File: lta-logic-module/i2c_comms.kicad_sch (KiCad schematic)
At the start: 9 parts

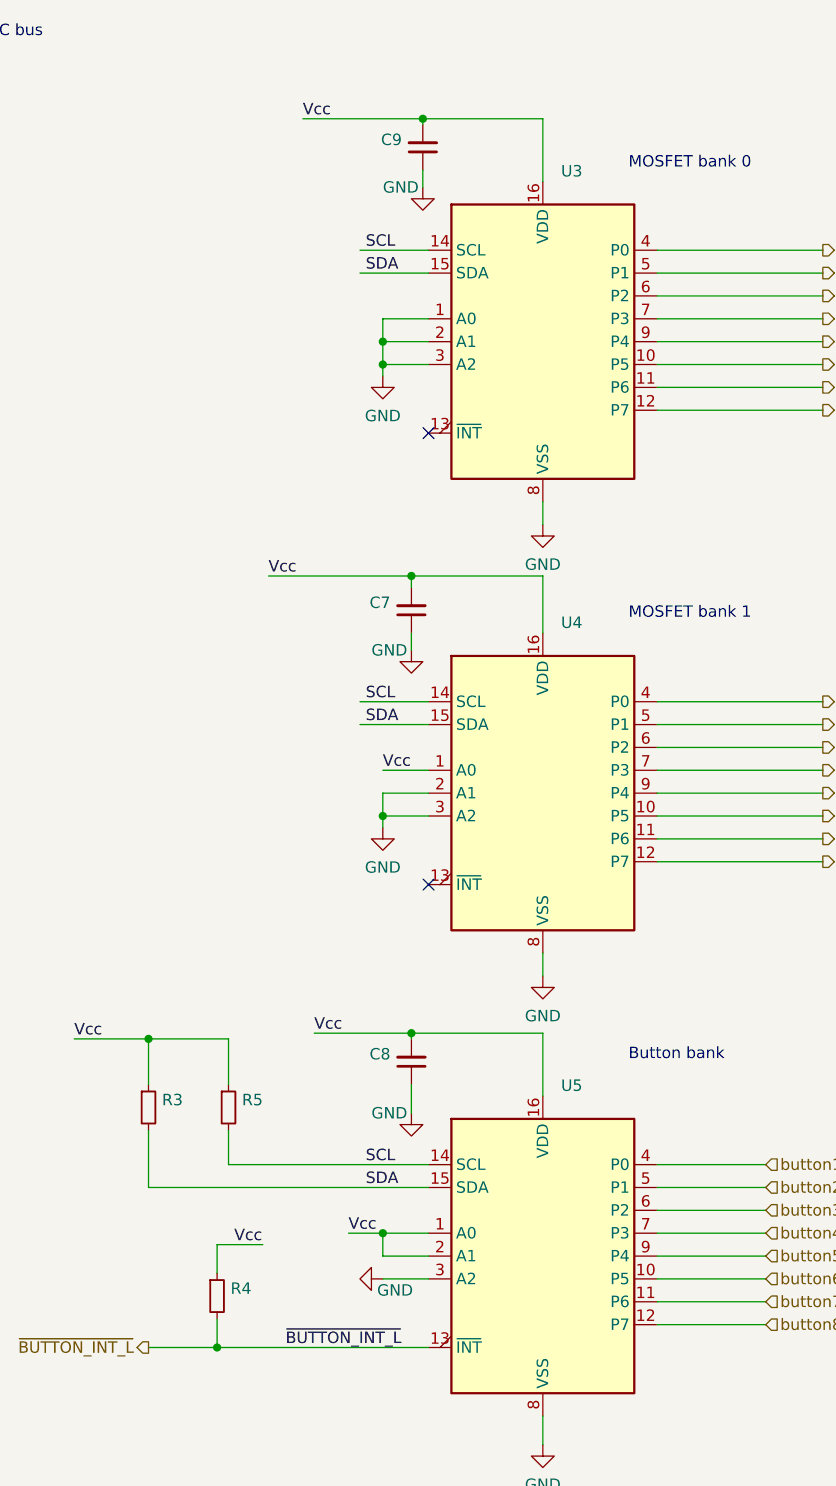
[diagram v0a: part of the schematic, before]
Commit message: Update logic module power budget from button LED measurements.
Button LEDs draw ~11mA each (98 mA total) empirically; not the ~20mA each
I initially guessed for estimating purposes.
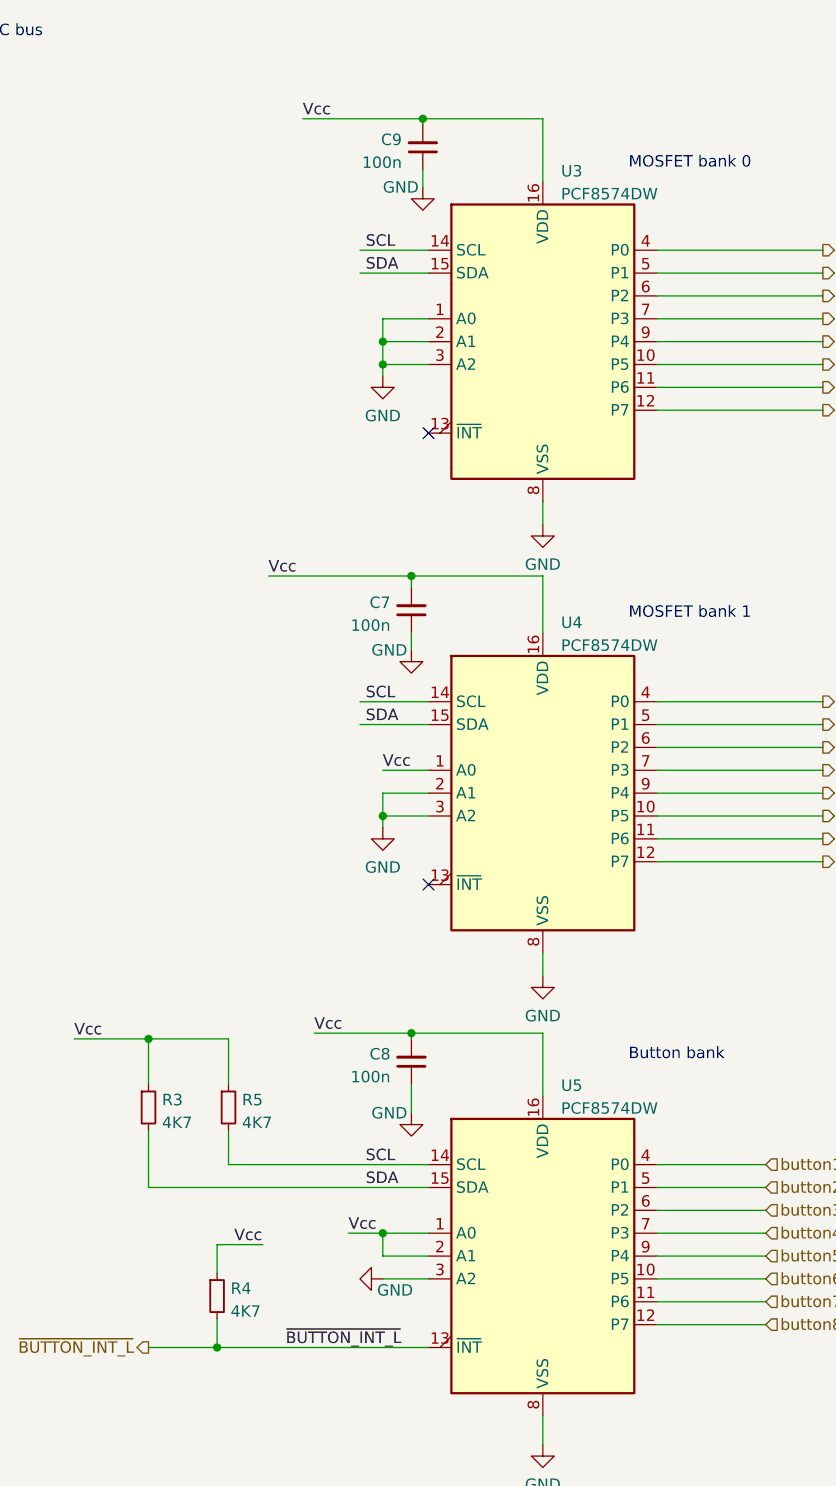
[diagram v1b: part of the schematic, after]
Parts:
- C7, C8, C9: value (none) -> 100n; footprint (none) -> Capacitor_SMD:C_0603_1608Metric
- R3, R4, R5: value (none) -> 4K7; footprint (none) -> Resistor_SMD:R_0603_1608Metric
- U3, U4, U5: value (none) -> PCF8574DW; footprint (none) -> Aaron_TI_Parts:TI_SOIC_DW0016A
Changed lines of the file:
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@@
       (effects (font (size 1.27 1.27)) (justify left))
     )
-    (property "Value" "" (id 1) (at 77.0636 137.5922 0)
-      (effects (font (size 1.27 1.27)) (justify left))
-    )
-    (property "Footprint" "" (id 2) (at 75.565 135.89 0)
+    (property "Value" "4K7" (id 1) (at 77.0636 137.5922 0)
+      (effects (font (size 1.27 1.27)) (justify left))
+    )
+    (property "Footprint" "Resistor_SMD:R_0603_1608Metric" (id 2) (at 75.565 135.89 0)
       (effects (font (size 1.27 1.27)) hide)
     )
@@
       (effects (font (size 1.27 1.27)) (justify right))
     )
-    (property "Value" "" (id 1) (at 93.5609 132.5058 0)
-      (effects (font (size 1.27 1.27)) (justify right))
-    )
-    (property "Footprint" "" (id 2) (at 95.885 130.81 0)
+    (property "Value" "100n" (id 1) (at 93.5609 132.5058 0)
+      (effects (font (size 1.27 1.27)) (justify right))
+    )
+    (property "Footprint" "Capacitor_SMD:C_0603_1608Metric" (id 2) (at 95.885 130.81 0)
       (effects (font (size 1.27 1.27)) hide)
     )
@@
       (effects (font (size 1.27 1.27)) (justify left))
     )
-    (property "Value" "" (id 1) (at 75.7936 158.5472 0)
-      (effects (font (size 1.27 1.27)) (justify left))
-    )
-    (property "Footprint" "" (id 2) (at 74.295 156.845 0)
+    (property "Value" "4K7" (id 1) (at 75.7936 158.5472 0)
+      (effects (font (size 1.27 1.27)) (justify left))
+    )
+    (property "Footprint" "Resistor_SMD:R_0603_1608Metric" (id 2) (at 74.295 156.845 0)
       (effects (font (size 1.27 1.27)) hide)
     )
@@
       (effects (font (size 1.27 1.27)) (justify right))
     )
-    (property "Value" "" (id 1) (at 93.5609 82.3408 0)
-      (effects (font (size 1.27 1.27)) (justify right))
-    )
-    (property "Footprint" "" (id 2) (at 95.885 80.645 0)
+    (property "Value" "100n" (id 1) (at 93.5609 82.3408 0)
+      (effects (font (size 1.27 1.27)) (justify right))
+    )
+    (property "Footprint" "Capacitor_SMD:C_0603_1608Metric" (id 2) (at 95.885 80.645 0)
       (effects (font (size 1.27 1.27)) hide)
     )
@@
       (effects (font (size 1.27 1.27)) (justify right))
     )
-    (property "Value" "" (id 1) (at 94.8309 30.9058 0)
-      (effects (font (size 1.27 1.27)) (justify right))
-    )
-    (property "Footprint" "" (id 2) (at 97.155 29.21 0)
+    (property "Value" "100n" (id 1) (at 94.8309 30.9058 0)
+      (effects (font (size 1.27 1.27)) (justify right))
+    )
+    (property "Footprint" "Capacitor_SMD:C_0603_1608Metric" (id 2) (at 97.155 29.21 0)
       (effects (font (size 1.27 1.27)) hide)
     )
@@
       (effects (font (size 1.27 1.27)) (justify left))
     )
-    (property "Value" "" (id 1) (at 112.5094 84.5621 0)
-      (effects (font (size 1.27 1.27)) (justify left))
-    )
-    (property "Footprint" "" (id 2) (at 110.49 100.965 0)
+    (property "Value" "PCF8574DW" (id 1) (at 112.5094 84.5621 0)
+      (effects (font (size 1.27 1.27)) (justify left))
+    )
+    (property "Footprint" "Aaron_TI_Parts:TI_SOIC_DW0016A" (id 2) (at 110.49 100.965 0)
       (effects (font (size 1.27 1.27)) hide)
     )
@@
       (effects (font (size 1.27 1.27)) (justify left))
     )
-    (property "Value" "" (id 1) (at 68.1736 137.5922 0)
-      (effects (font (size 1.27 1.27)) (justify left))
-    )
-    (property "Footprint" "" (id 2) (at 66.675 135.89 0)
+    (property "Value" "4K7" (id 1) (at 68.1736 137.5922 0)
+      (effects (font (size 1.27 1.27)) (justify left))
+    )
+    (property "Footprint" "Resistor_SMD:R_0603_1608Metric" (id 2) (at 66.675 135.89 0)
       (effects (font (size 1.27 1.27)) hide)
     )
@@
       (effects (font (size 1.27 1.27)) (justify left))
     )
-    (property "Value" "" (id 1) (at 112.5094 34.3971 0)
-      (effects (font (size 1.27 1.27)) (justify left))
-    )
-    (property "Footprint" "" (id 2) (at 110.49 50.8 0)
+    (property "Value" "PCF8574DW" (id 1) (at 112.5094 34.3971 0)
+      (effects (font (size 1.27 1.27)) (justify left))
+    )
+    (property "Footprint" "Aaron_TI_Parts:TI_SOIC_DW0016A" (id 2) (at 110.49 50.8 0)
       (effects (font (size 1.27 1.27)) hide)
     )
@@
       (effects (font (size 1.27 1.27)) (justify left))
     )
-    (property "Value" "" (id 1) (at 112.5094 135.9971 0)
-      (effects (font (size 1.27 1.27)) (justify left))
-    )
-    (property "Footprint" "" (id 2) (at 110.49 152.4 0)
-      (effects (font (size 1.27 1.27)) hide)
-    )
+    (property "Value" "PCF8574DW" (id 1) (at 112.5094 135.9971 0)
+      (effects (font (size 1.27 1.27)) (justify left))
+    )
+    (property "Footprint" "Aaron_TI_Parts:TI_SOIC_DW0016A" (id 2) (at 110.49 152.4 0)
+      (effects (font (size 1.27 1.27)) hide)
+    )
